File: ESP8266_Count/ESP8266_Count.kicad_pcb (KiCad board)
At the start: 2 copper layers, 43.7 x 26.1 mm, 25 parts, among them J1 PMG, J2 String1, J3 OLED, SW1 SW_Push, U1 AMS1117-3.3, U2 AMS1117-5.0, U3 ESP-12E, U4 74AHCT1G125, U5 ACS706xLC-05C

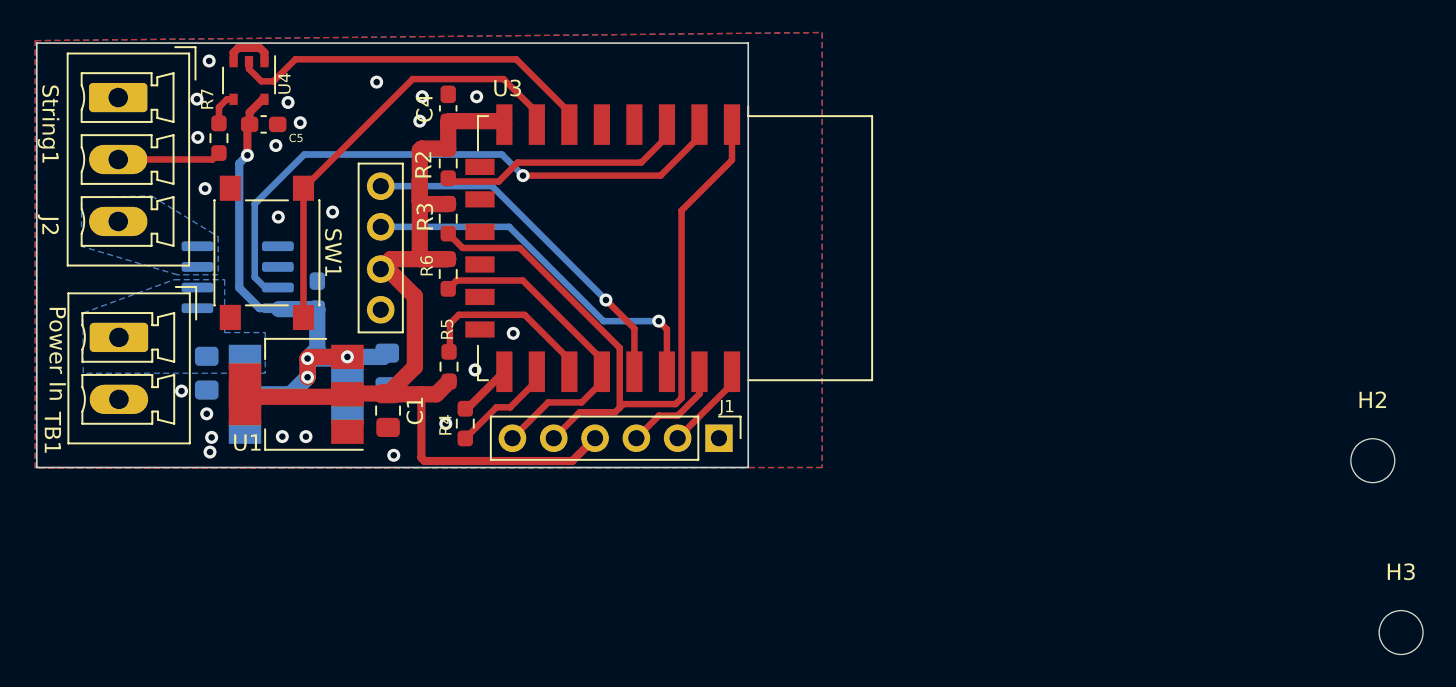
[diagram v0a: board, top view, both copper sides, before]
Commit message: added dmx to stepper
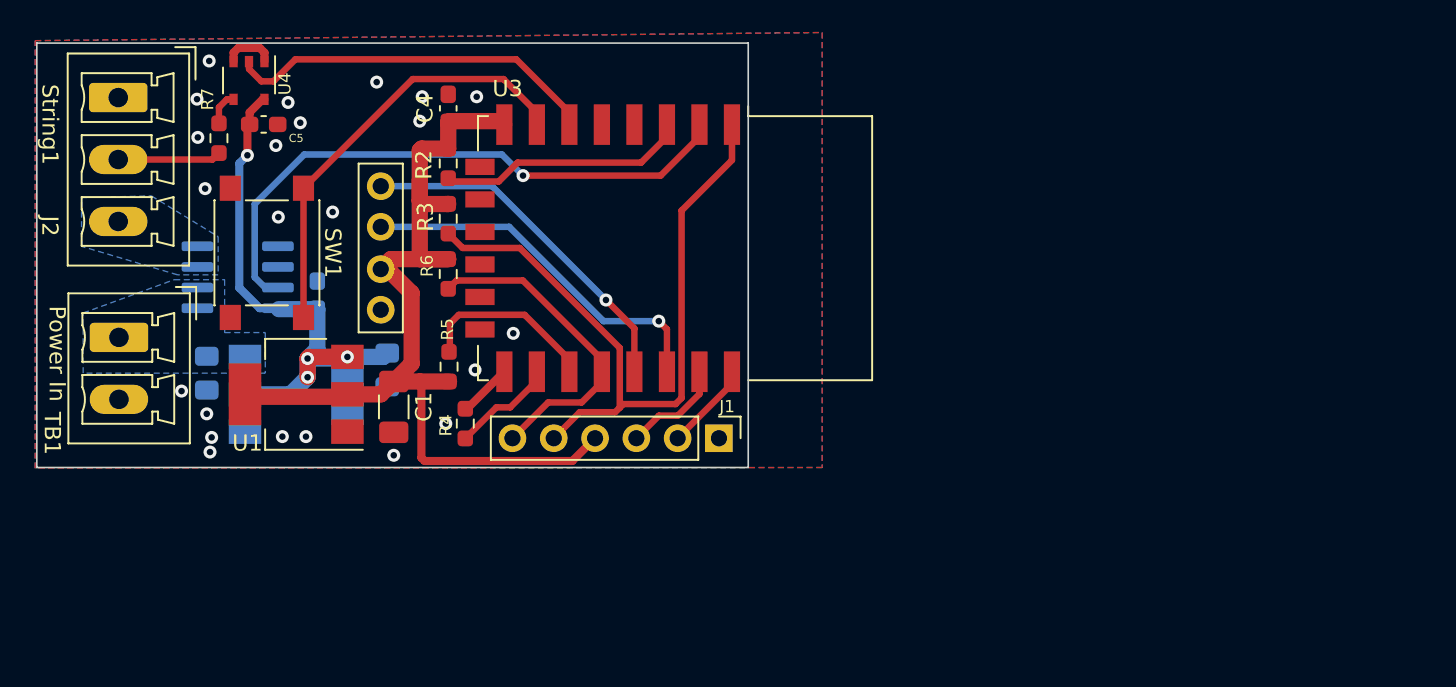
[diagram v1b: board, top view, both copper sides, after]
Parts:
- removed H2, H3: MountingHole, MountingHole:MountingHole_2.7mm_M2.5
- C1: footprint Capacitor_SMD:C_0805_2012Metric_Pad1.18x1.45mm_HandSolder -> Capacitor_SMD:C_1206_3216Metric_Pad1.33x1.80mm_HandSolder
- moved C1 0.42 mm to (131.9, 81.3)

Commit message: minor fixes
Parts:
- moved U4 0.30 mm to (123.0, 61.5)
- moved R7 0.25 mm to (121.2, 65.0)
- moved C5 0.20 mm to (123.9, 64.1)
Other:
- board text added: "12V"
- board text added: "3.3V"
- board text added: "Data"
- board text added: "GND"
- board text added: "IO0"
- board text added: "RST"
- board text added: "RX"
- board text added: "TX"
